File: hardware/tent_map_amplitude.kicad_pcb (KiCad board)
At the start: 4 copper layers, 24 parts, among them J1 22-23-2021, U1 LM339AN, U2 TL082IP, U3 TL082IP

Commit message: Complete PCB (unreviewed)
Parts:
- removed J1: 22-23-2021, digikey-footprints:PinHeader_1x2_P2.54mm_Drill1.02mm
- added ?: , , F.Cu at (67.5, 87.9)
- added C10: 0.1u, Capacitor_SMD:C_0805_2012Metric_Pad1.18x1.45mm_HandSolder, F.Cu at (99.3, 82.7)
- added C11: 0.1u, Capacitor_SMD:C_0805_2012Metric_Pad1.18x1.45mm_HandSolder, F.Cu at (85.7, 91.7)
- added C12: 0.1u, Capacitor_SMD:C_0805_2012Metric_Pad1.18x1.45mm_HandSolder, F.Cu at (94.7, 63.5)
- added C13: 0.1u, Capacitor_SMD:C_0805_2012Metric_Pad1.18x1.45mm_HandSolder, F.Cu at (89.1, 96.7)
- added C14: 0.1u, Capacitor_SMD:C_0805_2012Metric_Pad1.18x1.45mm_HandSolder, F.Cu at (77.7, 67.6)
- added C15: 0.1u, Capacitor_SMD:C_0805_2012Metric_Pad1.18x1.45mm_HandSolder, F.Cu at (107.3, 88.7)
- added C16: 0.1u, Capacitor_THT:C_Rect_L10.3mm_W5.0mm_P7.50mm_MKS4, F.Cu at (118.2, 76.7)
- added C17: 0.1u, Capacitor_THT:C_Rect_L10.3mm_W5.0mm_P7.50mm_MKS4, F.Cu at (105.9, 76.5)
- added C18: 0.1u, Capacitor_THT:C_Rect_L10.3mm_W5.0mm_P7.50mm_MKS4, F.Cu at (89.7, 76.5)
- added C8: 10u, Capacitor_THT:CP_Radial_D5.0mm_P2.00mm, F.Cu at (68.4, 77.2)
- added C9: 10u, Capacitor_THT:CP_Radial_D5.0mm_P2.00mm, F.Cu at (117.6, 58.2)
- added TP10: Vclock, TestPoint:TestPoint_Bridge_Pitch2.54mm_Drill1.0mm, F.Cu at (78.6, 58.0)
- added TP11: Vsn+1, TestPoint:TestPoint_Bridge_Pitch2.54mm_Drill1.0mm, F.Cu at (101.5, 58.0)
- added TP12: Vclock-, TestPoint:TestPoint_Bridge_Pitch2.54mm_Drill1.0mm, F.Cu at (71.0, 58.0)
- added TP13: Vsn+1/2, TestPoint:TestPoint_Bridge_Pitch2.54mm_Drill1.0mm, F.Cu at (93.9, 58.0)
- added TP14: Vsn, TestPoint:TestPoint_Bridge_Pitch2.54mm_Drill1.0mm, F.Cu at (86.3, 55.4)
- added TP3: GND, TestPoint:TestPoint_Bridge_Pitch2.54mm_Drill1.0mm, F.Cu at (88.5, 109.2)
- added TP4: V+, TestPoint:TestPoint_Bridge_Pitch2.54mm_Drill1.0mm, F.Cu at (75.8, 109.2)
- added TP5: V-, TestPoint:TestPoint_Bridge_Pitch2.54mm_Drill1.0mm, F.Cu at (100.6, 109.2)
- added TP6: Vbuffer, TestPoint:TestPoint_Bridge_Pitch2.54mm_Drill1.0mm, F.Cu at (92.7, 105.0)
- added TP7: Vctrl, TestPoint:TestPoint_Bridge_Pitch2.54mm_Drill1.0mm, F.Cu at (100.7, 105.1)
- added TP8: ana_in, TestPoint:TestPoint_Bridge_Pitch2.54mm_Drill1.0mm, F.Cu at (68.8, 105.4)
- added TP9: Vctrl, TestPoint:TestPoint_Bridge_Pitch2.54mm_Drill1.0mm, F.Cu at (68.4, 85.6)
- added U4: LF398_DIP8, digikey-footprints:DIP-8_W7.62mm, F.Cu at (113.1, 63.5)
- added U5: LF398_DIP8, digikey-footprints:DIP-8_W7.62mm, F.Cu at (98.3, 63.5)
- added U6: LF398_DIP8, digikey-footprints:DIP-8_W7.62mm, F.Cu at (82.0, 63.8)
- RV1: footprint Potentiometer_THT:Potentiometer_Bourns_3296Y_Vertical -> Potentiometer_THT:Potentiometer_Bourns_3296W_Vertical
- TP1: value TestPoint_2Pole -> Vc; footprint TestPoint:TestPoint_Bridge_Pitch2.54mm_Drill0.7mm -> TestPoint:TestPoint_Bridge_Pitch2.54mm_Drill1.0mm
- TP2: value TestPoint_2Pole -> ana_out; footprint TestPoint:TestPoint_Bridge_Pitch2.54mm_Drill0.7mm -> TestPoint:TestPoint_Bridge_Pitch2.54mm_Drill1.0mm
- moved D2 177.1 mm to (115.6, 103.2), turned to 180 degrees
- moved C4 166.3 mm to (119.6, 100.7), turned to 90 degrees
- moved U3 160.0 mm to (116.1, 92.0), turned to 270 degrees
- moved RV1 156.4 mm to (108.0, 109.4), turned to 180 degrees
- moved D1 155.3 mm to (110.2, 82.2)
- moved TP1 152.5 mm to (111.7, 58.0), turned to 90 degrees
- moved U2 144.9 mm to (90.3, 86.4)
- moved U1 144.8 mm to (75.2, 87.7)
- moved C2 140.1 mm to (109.4, 71.1)
- moved R6 136.7 mm to (111.0, 88.5), turned to 270 degrees
- moved C1 135.2 mm to (86.6, 102.8), turned to 270 degrees
- moved R4 133.9 mm to (102.5, 90.5), turned to 270 degrees
- moved R2 133.0 mm to (102.0, 94.5), turned to 180 degrees
- moved TP2 130.6 mm to (69.6, 63.8)
- moved C3 130.5 mm to (109.4, 63.5), turned to 180 degrees
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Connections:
- TP1 pad 1: Net-(R1-Pad2) -> Net-(C1-Pad1)
- TP2 pad 1: Net-(TP2-Pad1) -> Net-(R1-Pad2)
- U1 pad 7: Net-(TP2-Pad1) -> Net-(TP8-Pad1)
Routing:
- net Net-(C1-Pad1): track 0.00 -> 86.7 mm, vias 0 -> 1
- net Net-(R6-Pad2): track 0.00 -> 61.9 mm
- net Net-(TP10-Pad1): track 0.00 -> 48.9 mm
- net Net-(TP12-Pad1): track 0.00 -> 39.7 mm
- net Net-(TP13-Pad1): track 0.00 -> 37.8 mm
- net Net-(TP11-Pad1): track 0.00 -> 36.1 mm, vias 0 -> 1
- net Net-(D1-Pad1): track 0.00 -> 35.5 mm
- net V+: track 0.00 -> 32.8 mm, vias 0 -> 3
- net Net-(RV1-Pad2): track 0.00 -> 29.5 mm
- net Net-(R1-Pad2): track 0.00 -> 23.7 mm
- net Net-(R5-Pad1): track 0.00 -> 23.6 mm
- net Net-(TP14-Pad1): track 0.00 -> 18.4 mm
- net V-: track 0.00 -> 18.3 mm, vias 0 -> 1
- net GND: track 0.00 -> 16.9 mm, vias 0 -> 14
- net Net-(R4-Pad2): track 0.00 -> 16.1 mm
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- added copper zone on In1.Cu, net GND
- added copper zone on In2.Cu, net V+
- added copper zone on B.Cu, net V-
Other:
- board outline added: 56.4 x 60.2 mm
- board text added: "Chaotic Crew senior design 2020 tent map CRNG"

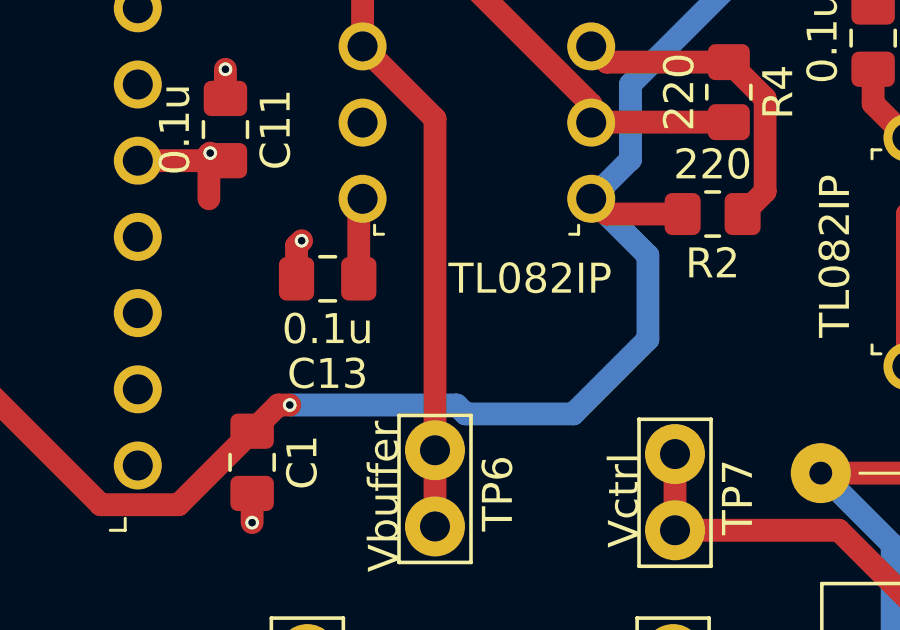
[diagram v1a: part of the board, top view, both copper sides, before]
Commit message: Reroute trace
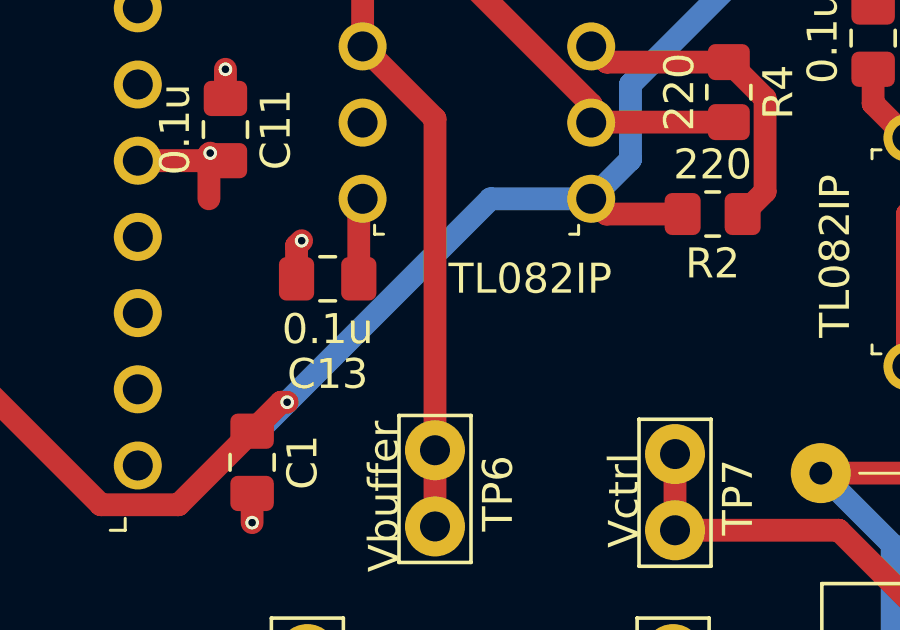
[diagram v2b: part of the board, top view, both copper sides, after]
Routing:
- net Net-(C1-Pad1): track 86.7 -> 82.0 mm
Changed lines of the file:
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@@
     (thickness 1.6002)
     (drawings 5)
-    (tracks 195)
+    (tracks 192)
     (zones 0)
     (modules 50)
@@
   (segment (start 84.162999 104.228801) (end 81.572001 104.228801) (width 0.762) (layer Front) (net 2))
   (segment (start 86.614 101.7778) (end 84.162999 104.228801) (width 0.762) (layer Front) (net 2))
-  (segment (start 99.806579 95.920379) (end 97.917 94.0308) (width 0.762) (layer Back) (net 2))
-  (segment (start 99.806579 98.714379) (end 99.806579 95.920379) (width 0.762) (layer Back) (net 2))
-  (segment (start 99.806579 98.714379) (end 97.320001 101.200957) (width 0.762) (layer Back) (net 2))
-  (segment (start 93.433841 100.904799) (end 87.868001 100.904799) (width 0.762) (layer Back) (net 2))
-  (segment (start 93.729999 101.200957) (end 93.433841 100.904799) (width 0.762) (layer Back) (net 2))
-  (segment (start 97.320001 101.200957) (end 93.729999 101.200957) (width 0.762) (layer Back) (net 2))
-  (via (at 87.868001 100.904799) (size 0.4572) (drill 0.254) (layers Front Back) (net 2))
-  (segment (start 87.487001 100.904799) (end 86.614 101.7778) (width 0.762) (layer Front) (net 2))
-  (segment (start 87.868001 100.904799) (end 87.487001 100.904799) (width 0.762) (layer Front) (net 2))
   (segment (start 114.414201 60.718601) (end 111.6584 57.9628) (width 0.762) (layer Front) (net 2))
   (segment (start 114.414201 67.297399) (end 114.414201 60.718601) (width 0.762) (layer Front) (net 2))
@@
   (segment (start 114.414201 69.913401) (end 114.414201 75.857199) (width 0.762) (layer Back) (net 2))
   (segment (start 113.1062 68.6054) (end 114.414201 69.913401) (width 0.762) (layer Back) (net 2))
+  (segment (start 97.917 94.0308) (end 94.5642 94.0308) (width 0.762) (layer Back) (net 2))
+  (segment (start 94.5642 94.0308) (end 87.7824 100.8126) (width 0.762) (layer Back) (net 2))
+  (segment (start 87.7824 100.8126) (end 87.0712 101.5238) (width 0.762) (layer Back) (net 2))
+  (via (at 87.7824 100.8126) (size 0.4572) (drill 0.254) (layers Front Back) (net 2))
+  (segment (start 87.5792 100.8126) (end 86.614 101.7778) (width 0.762) (layer Front) (net 2))
+  (segment (start 87.7824 100.8126) (end 87.5792 100.8126) (width 0.762) (layer Front) (net 2))
   (segment (start 95.758 71.12) (end 98.298 71.12) (width 0.762) (layer Front) (net 3))
   (segment (start 81.788 71.628) (end 82.042 71.374) (width 0.762) (layer Front) (net 3))

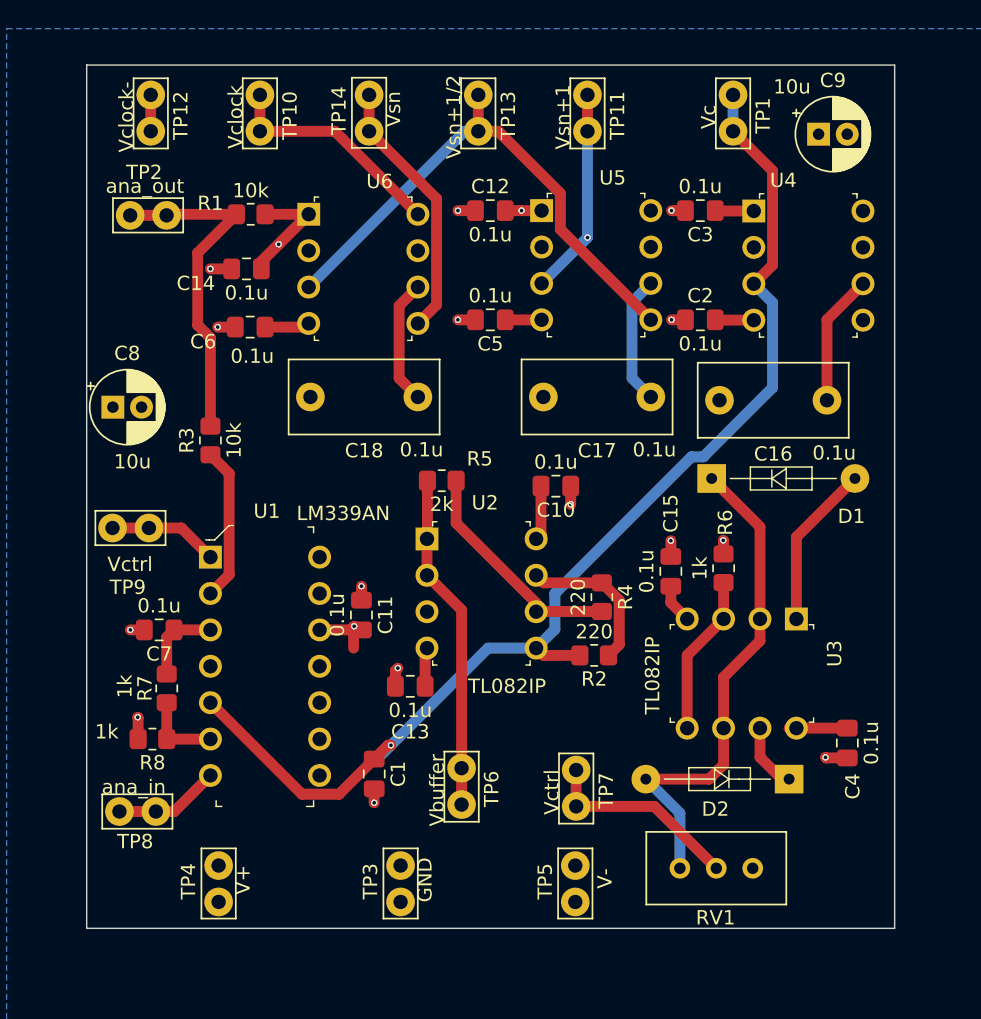
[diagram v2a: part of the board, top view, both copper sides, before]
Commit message: update pcb and schematic to have 3.3V input for interfacing with DE-10 nano
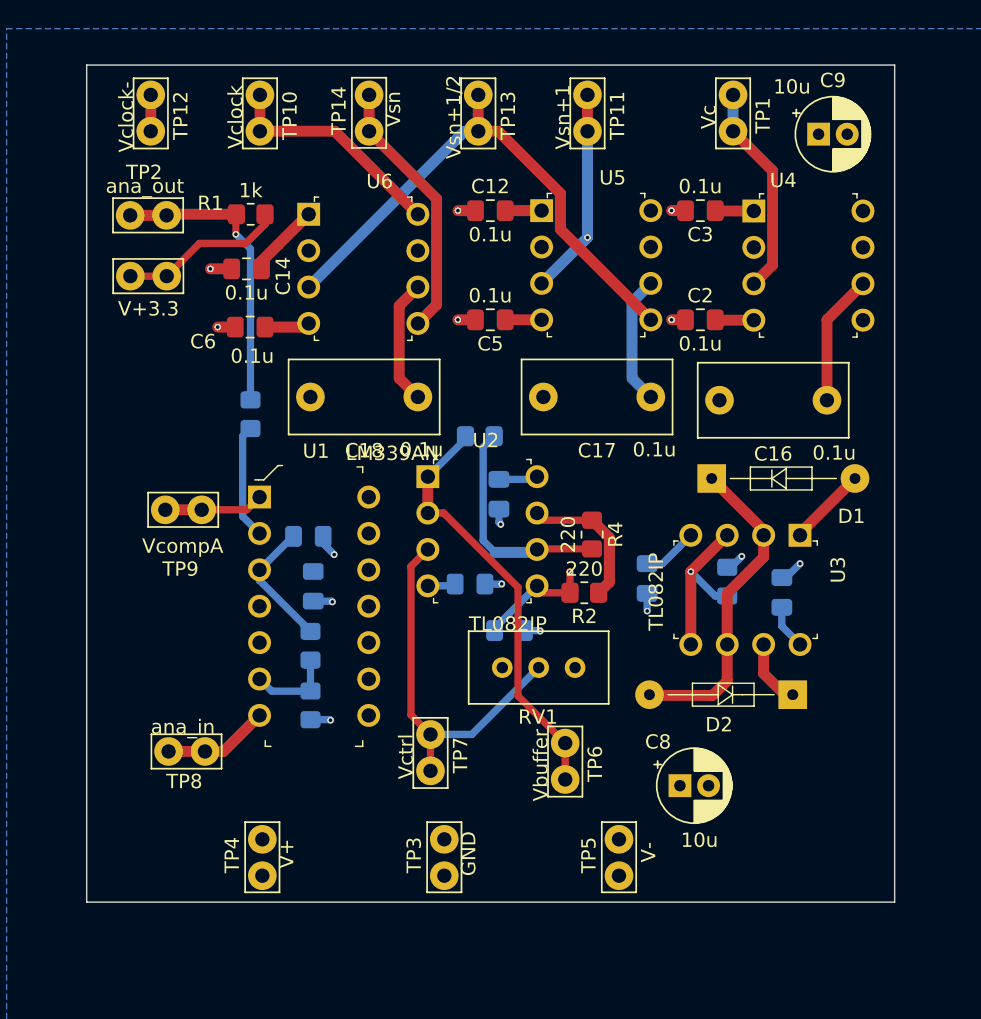
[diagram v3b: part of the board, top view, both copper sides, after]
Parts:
- removed ?: , 
- added TP15: V+3.3, TestPoint:TestPoint_Bridge_Pitch2.54mm_Drill1.0mm, F.Cu at (69.6, 68.1)
- C1, C10, C11, C13, C15, C4, C7, R5, R6, R7, R8: moved to B.Cu
- R1: value 10k -> 1k
- R3: value 10k -> 1k; moved to B.Cu
- TP9: value Vctrl -> VcompA
- moved C8 47.6 mm to (108.0, 103.6)
- moved RV1 18.7 mm to (95.6, 95.4)
- moved C1 13.8 mm to (96.1, 92.8), turned to 0 degrees
- moved C7 12.3 mm to (82.0, 86.2), turned to 0 degrees
- moved C4 11.5 mm to (115.1, 90.1), turned to 270 degrees
- moved R8 11.3 mm to (82.2, 98.0), turned to 270 degrees
- moved TP7 10.5 mm to (90.5, 102.6)
- moved R7 10.5 mm to (82.2, 93.9)
- moved C13 8.26 mm to (93.3, 89.6), turned to 180 degrees
- moved TP6 7.44 mm to (99.9, 103.2)
- moved D2 5.90 mm to (115.8, 97.3)
- moved U3 5.85 mm to (116.3, 86.2)
- moved TP8 5.42 mm to (72.3, 101.2)
- moved U1 5.42 mm to (78.6, 83.5)
- moved R4 4.42 mm to (101.8, 86.1)
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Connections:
- R1 pad 1: V+ -> +3V3
- R5 pad 1: Net-(R5-Pad1) -> Net-(R4-Pad2)
- R5 pad 2: Net-(R4-Pad2) -> Net-(R5-Pad2)
- TP6 pad 1: Net-(R5-Pad1) -> Net-(R5-Pad2)
- U2 pad 1: Net-(R5-Pad1) -> Net-(R5-Pad2)
- U2 pad 2: Net-(R5-Pad1) -> Net-(R5-Pad2)
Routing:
- net Net-(R5-Pad2): track 0.00 -> 29.7 mm
- net Net-(R5-Pad1): track 23.6 -> 0.00 mm
- net +3V3: track 0.00 -> 11.6 mm
- net Net-(C1-Pad1): track 82.0 -> 70.6 mm
- net Net-(R6-Pad2): track 61.9 -> 51.7 mm, vias 0 -> 1
- net Net-(D1-Pad2): track 11.5 -> 5.78 mm
- net V-: track 18.3 -> 14.4 mm, vias 1 -> 0
- net Net-(RV1-Pad2): track 29.5 -> 26.0 mm
- net Net-(R1-Pad2): track 23.7 -> 20.8 mm, vias 0 -> 1
- net Net-(R3-Pad1): track 10.8 -> 8.04 mm
- net Net-(D1-Pad1): track 35.5 -> 32.9 mm
- net V+: track 32.8 -> 31.4 mm, vias 3 -> 1
- net GND: track 16.9 -> 17.9 mm
- net Net-(R2-Pad1): track 10.7 -> 9.92 mm
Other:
- board size 56.4 x 60.2 mm -> 56.4 x 58.4 mm

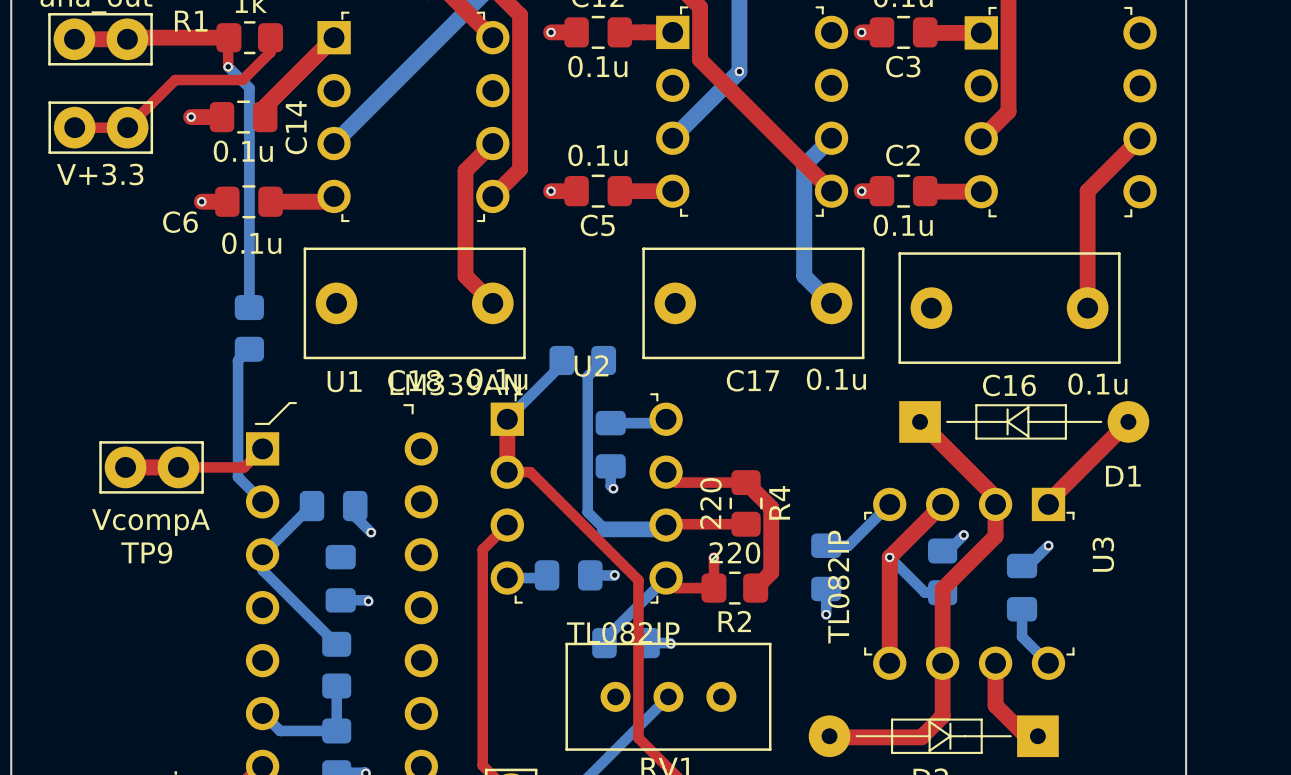
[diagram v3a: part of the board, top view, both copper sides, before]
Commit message: use 3.3v for logic level for input comparator
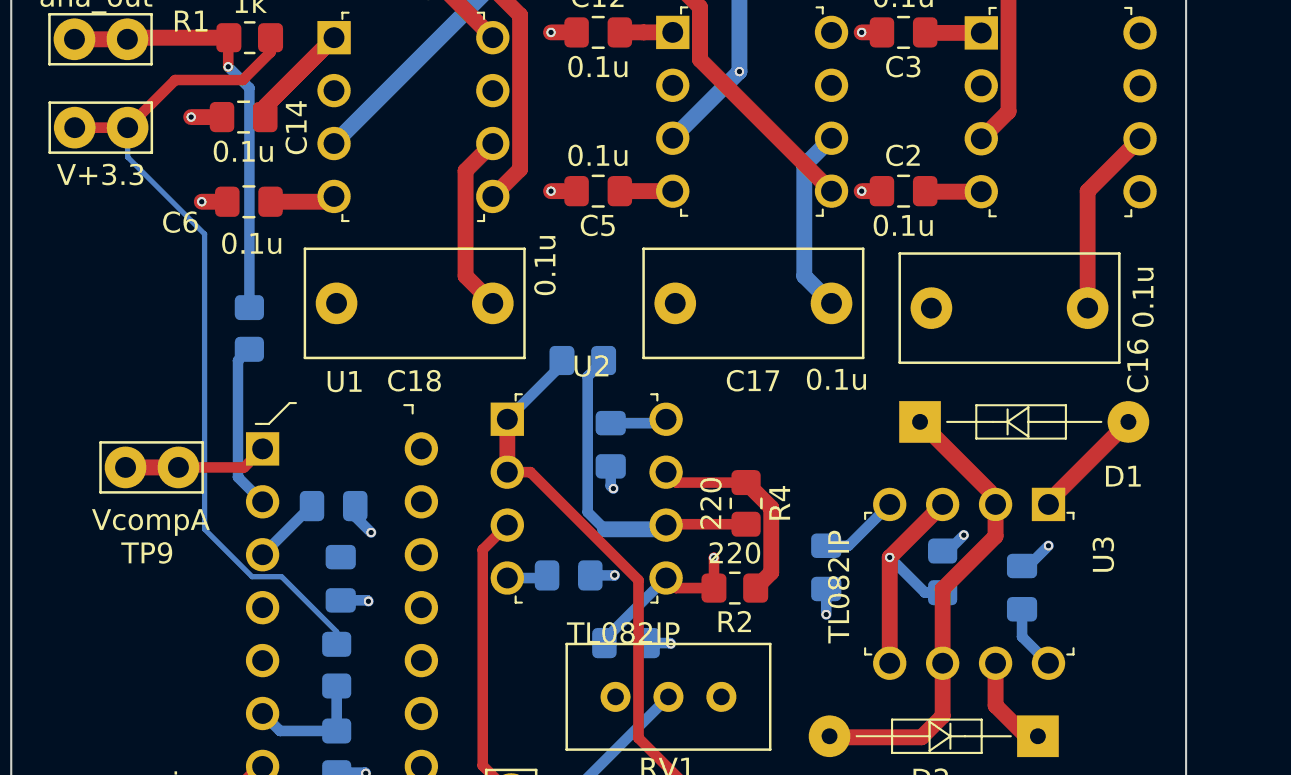
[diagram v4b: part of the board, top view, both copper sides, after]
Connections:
- R7 pad 1: V+ -> +3V3
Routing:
- net +3V3: track 11.6 -> 41.4 mm
- net V+: track 31.4 -> 25.6 mm
